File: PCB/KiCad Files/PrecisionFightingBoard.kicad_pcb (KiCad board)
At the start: 2 copper layers, 12 parts, among them J1 Conn_01x04_Male, J10 ST01x05, J2 Screw_Terminal_01x04, J6 Conn_02x10_Odd_Even, J7 ST01x05, J8 ST01x05, J9 ST01x05, U1 Teensy4.0

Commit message: Wired
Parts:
- added J3: Conn_01x14_Socket, Connector_PinSocket_2.54mm:PinSocket_1x14_P2.54mm_Vertical, F.Cu at (160.0, 58.4)
- added J4: Conn_01x14_Socket, Connector_PinSocket_2.54mm:PinSocket_1x14_P2.54mm_Vertical, F.Cu at (160.0, 73.7)
- moved J7 55.9 mm to (152.4, 48.3)
- moved J10 50.8 mm to (99.1, 48.3)
- moved J8 19.7 mm to (134.0, 48.3)
- moved J9 15.2 mm to (116.8, 48.3)
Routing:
- net /GND: track 0.00 -> 170.6 mm
- net /5V: track 0.00 -> 98.6 mm
- net /R3: track 0.00 -> 86.7 mm
- net /LT: track 0.00 -> 85.2 mm
- net /LEFT: track 0.00 -> 81.6 mm
- net /L3: track 0.00 -> 80.3 mm
- net /RT: track 0.00 -> 78.3 mm
- net /A: track 0.00 -> 75.4 mm
- net /RIGHT: track 0.00 -> 74.7 mm
- net /DOWN: track 0.00 -> 74.2 mm
- net /B: track 0.00 -> 73.1 mm
- net /START: track 0.00 -> 72.9 mm
- net /UP: track 0.00 -> 71.2 mm
- net /HOME: track 0.00 -> 70.8 mm
- net /RB: track 0.00 -> 70.3 mm
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
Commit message: add gerber files
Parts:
- moved J8 0.67 mm to (134.7, 48.2)
- moved J10 0.21 mm to (98.9, 48.3)
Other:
- board outline added: 97 x 48 mm
- board text added: "UNIT-00 PROTOTYPE"
- board text added: "github.com/ioridev/Precision-Fighting-Board"

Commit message: update pcb
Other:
- board text added: "8000Hz Ready"
- board text added: "Precision Fighting Board"
- board text removed: "UNIT-00 PROTOTYPE"

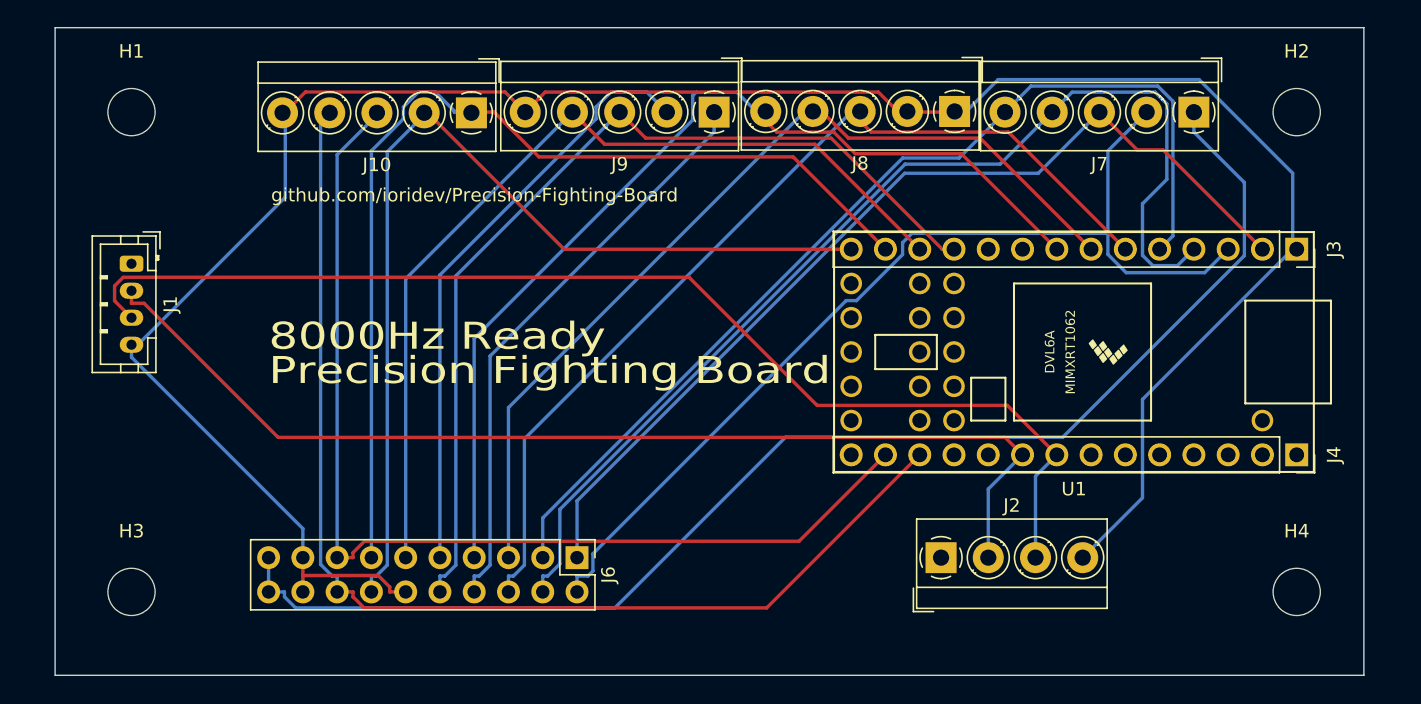
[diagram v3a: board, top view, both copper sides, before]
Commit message: Added rounded corners to the edges of the outline
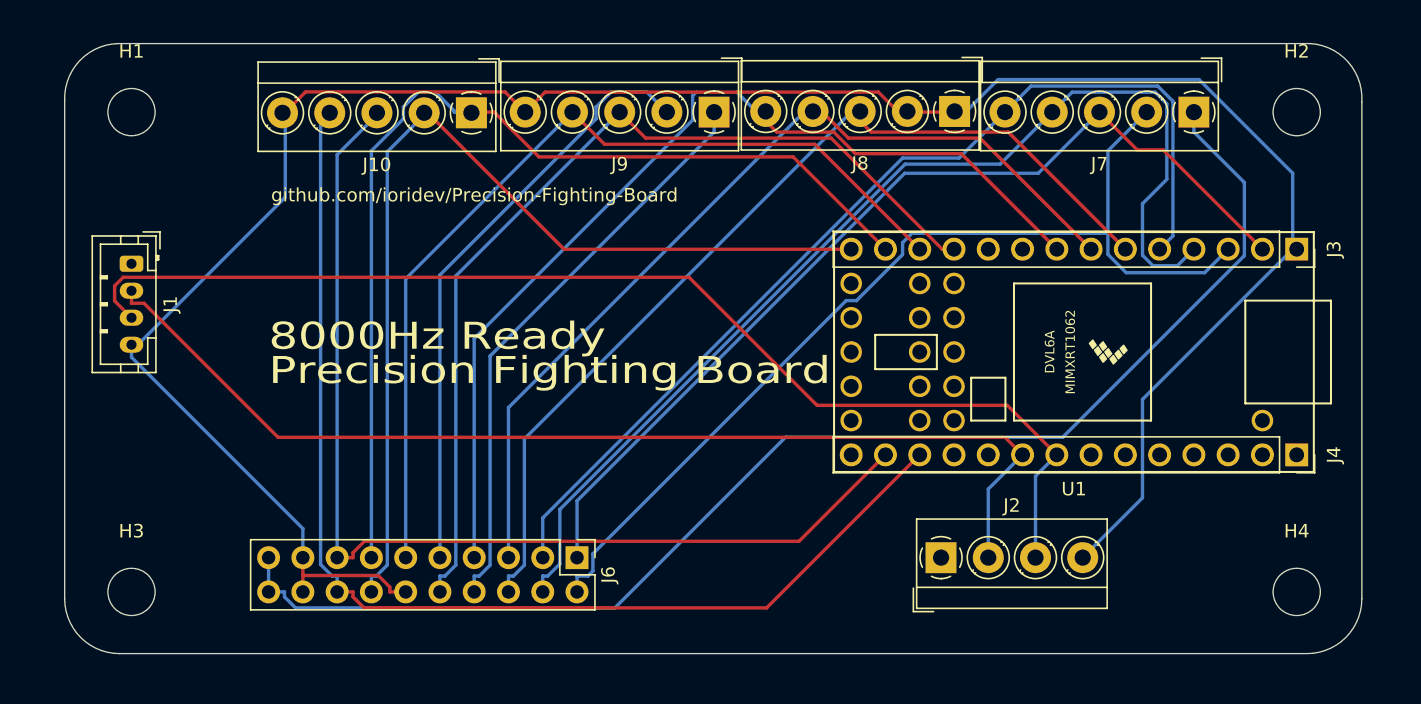
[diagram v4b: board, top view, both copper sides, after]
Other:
- board size 97 x 48 mm -> 96.1 x 45.2 mm
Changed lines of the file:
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@@
     )
   )
-  (gr_rect (start 68 42) (end 165 90)
-    (stroke (width 0.1) (type default)) (fill none) (layer "Edge.Cuts"))
+  (gr_arc (start 164.846 84.328) (mid 163.655682 87.201682) (end 160.782 88.392)
+    (stroke (width 0.05) (type solid)) (layer "Edge.Cuts"))
+  (gr_arc (start 72.771 88.392) (mid 69.897318 87.201682) (end 68.707 84.328)
+    (stroke (width 0.05) (type solid)) (layer "Edge.Cuts"))
+  (gr_line (start 68.707 84.328) (end 68.707 47.371)
+    (stroke (width 0.05) (type solid)) (layer "Edge.Cuts"))
+  (gr_line (start 160.782 88.392) (end 72.771 88.392)
+    (stroke (width 0.05) (type solid)) (layer "Edge.Cuts"))
+  (gr_arc (start 68.707 47.371) (mid 69.807515 44.460121) (end 72.644 43.18)
+    (stroke (width 0.05) (type solid)) (layer "Edge.Cuts"))
+  (gr_line (start 72.644 43.18) (end 161.036 43.18)
+    (stroke (width 0.05) (type solid)) (layer "Edge.Cuts"))
+  (gr_line (start 164.846 47.498) (end 164.846 84.328)
+    (stroke (width 0.05) (type solid)) (layer "Edge.Cuts"))
+  (gr_arc (start 161.036 43.18) (mid 163.835287 44.549923) (end 164.846 47.498)
+    (stroke (width 0.05) (type solid)) (layer "Edge.Cuts"))
   (gr_rect (start 165 42) (end 165 42)
     (stroke (width 0.1) (type default)) (fill none) (layer "Edge.Cuts"))

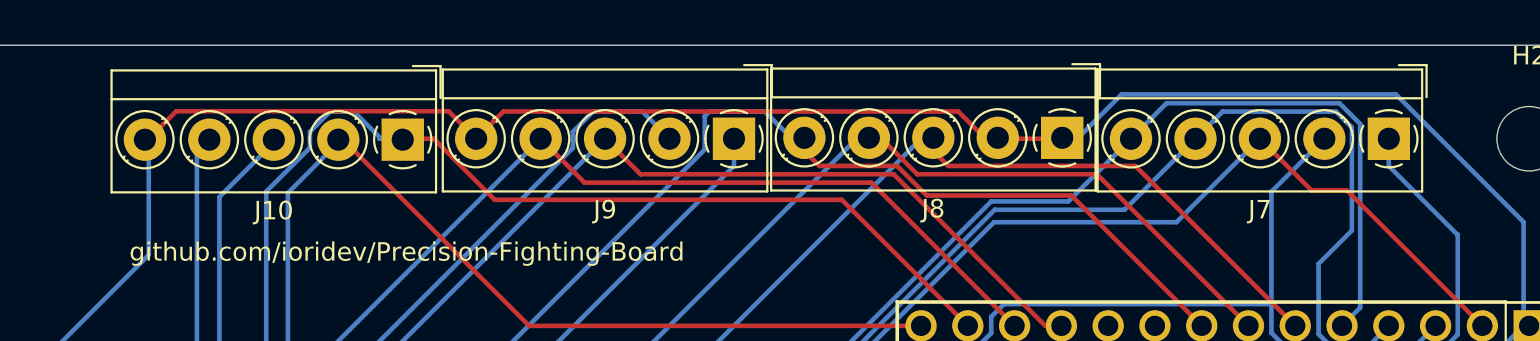
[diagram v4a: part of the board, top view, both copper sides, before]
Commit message: Changed 4-pin screw terminal to 3-pin.
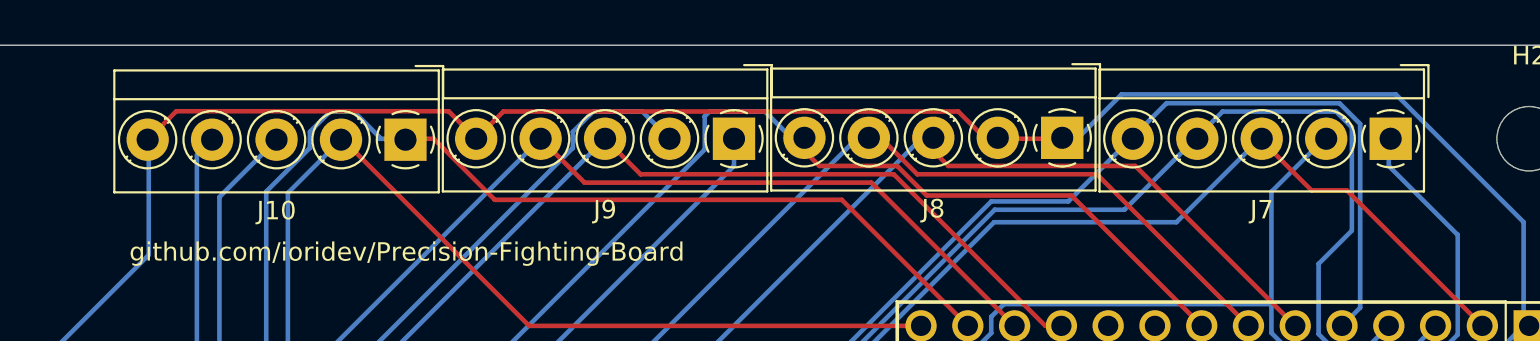
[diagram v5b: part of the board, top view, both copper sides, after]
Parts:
- moved J10 0.15 mm to (99.0, 48.3)
- moved J7 0.10 mm to (152.5, 48.3)
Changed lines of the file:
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@@
   )
   (footprint "TerminalBlock_MetzConnect:TerminalBlock_MetzConnect_Type059_RT06305HBWC_1x05_P3.50mm_Horizontal" (layer "F.Cu")
-    (at 98.8516 48.3108 180)
+    (at 99 48.3108 180)
     (descr "terminal block Metz Connect Type059_RT06305HBWC, 5 pins, pitch 3.5mm, size 17.5x6.5mm^2, drill diamater 1.2mm, pad diameter 2.3mm, see http://www.metz-connect.com/de/system/files/productfiles/Datenblatt_310591_RT063xxHBWC_OFF-022684T.pdf, script-generated using https://github.com/pointhi/kicad-footprint-generator/scripts/TerminalBlock_MetzConnect")
     (tags "THT terminal block Metz Connect Type059_RT06305HBWC pitch 3.5mm size 17.5x6.5mm^2 drill 1.2mm pad 2.3mm")
@@
   )
   (footprint "TerminalBlock_MetzConnect:TerminalBlock_MetzConnect_Type059_RT06305HBWC_1x05_P3.50mm_Horizontal" (layer "F.Cu")
-    (at 152.4 48.26 180)
+    (at 152.5 48.26 180)
     (descr "terminal block Metz Connect Type059_RT06305HBWC, 5 pins, pitch 3.5mm, size 17.5x6.5mm^2, drill diamater 1.2mm, pad diameter 2.3mm, see http://www.metz-connect.com/de/system/files/productfiles/Datenblatt_310591_RT063xxHBWC_OFF-022684T.pdf, script-generated using https://github.com/pointhi/kicad-footprint-generator/scripts/TerminalBlock_MetzConnect")
     (tags "THT terminal block Metz Connect Type059_RT06305HBWC pitch 3.5mm size 17.5x6.5mm^2 drill 1.2mm pad 2.3mm")

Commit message: Updated wiring.
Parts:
- removed J2: Screw_Terminal_01x04, TerminalBlock_MetzConnect:TerminalBlock_MetzConnect_Type059_RT06304HBWC_1x04_P3.50mm_Horizontal
- added J5: Screw_Terminal_01x03, TerminalBlock_MetzConnect:TerminalBlock_MetzConnect_Type059_RT06303HBWC_1x03_P3.50mm_Horizontal, F.Cu at (73.4, 58.0)
- moved J1 60.5 mm to (129.4, 82.9), turned to 0 degrees
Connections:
- J1 pad 1: unconnected-(J1-Pin_1-Pad1) -> /BACK
- J7 pad 1: /5V -> /GND
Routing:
- net /5V: track 98.6 -> 2.54 mm
- net /HOME: track 70.8 -> 145.1 mm
- net /Y: track 44.5 -> 76.2 mm
- net /X: track 43.1 -> 68.0 mm
- net /BACK: track 67.6 -> 90.7 mm
- net /LT: track 85.2 -> 100.9 mm
- net /RT: track 78.3 -> 87.4 mm, vias 0 -> 1
- net /UP: track 71.2 -> 79.9 mm
- net /GND: track 170.6 -> 176.6 mm
- net /LEFT: track 81.6 -> 86.7 mm
- net /RIGHT: track 74.7 -> 79.7 mm
- net /B: track 73.1 -> 76.7 mm
- net /L3: track 80.3 -> 83.7 mm, vias 0 -> 1
- net /DOWN: track 74.2 -> 77.3 mm
- net /LB: track 68.1 -> 68.5 mm, vias 0 -> 1
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- added copper zone on F.Cu, net /GND

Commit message: add label
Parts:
- added G***: LOGO, logo:iori_logo, F.Cu at (150.3, 83.7)
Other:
- board text added: "A"
- board text added: "B"
- board text added: "BAKC"
- board text added: "DESIGNED BY"
- board text added: "DOWN"
- board text added: "GND"
- board text added: "HOME"
- board text added: "LB"
- board text added: "LEFT"
- board text added: "LT"
- board text added: "RB"
- board text added: "RIGHT"
- board text added: "RT"
- board text added: "START"
- board text added: "UP"
- board text added: "X"
- board text added: "Y"

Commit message: fix pcb
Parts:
- removed J3, J4: Conn_01x14_Socket, Connector_PinSocket_2.54mm:PinSocket_1x14_P2.54mm_Vertical
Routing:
- net /X: track 68.0 -> 65.0 mm
- net /GND: track 176.6 -> 177.8 mm
- net /Y: track 76.2 -> 77.4 mm
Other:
- board text added: "L3"
- board text added: "R3"
